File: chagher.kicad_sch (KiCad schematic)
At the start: 16 parts, among them Q2 AO3401A, U6 CN3763

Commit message: DRC check
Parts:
- L2: footprint Inductor_SMD:L_TDK_VLS6045EX_VLS6045AF -> Inductor_SMD:L_TechFuse_SL0624
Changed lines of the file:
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@@
 			)
 		)
-		(property "Footprint" "Inductor_SMD:L_TDK_VLS6045EX_VLS6045AF"
+		(property "Footprint" "Inductor_SMD:L_TechFuse_SL0624"
 			(at 178.562 69.85 0)
 			(effects

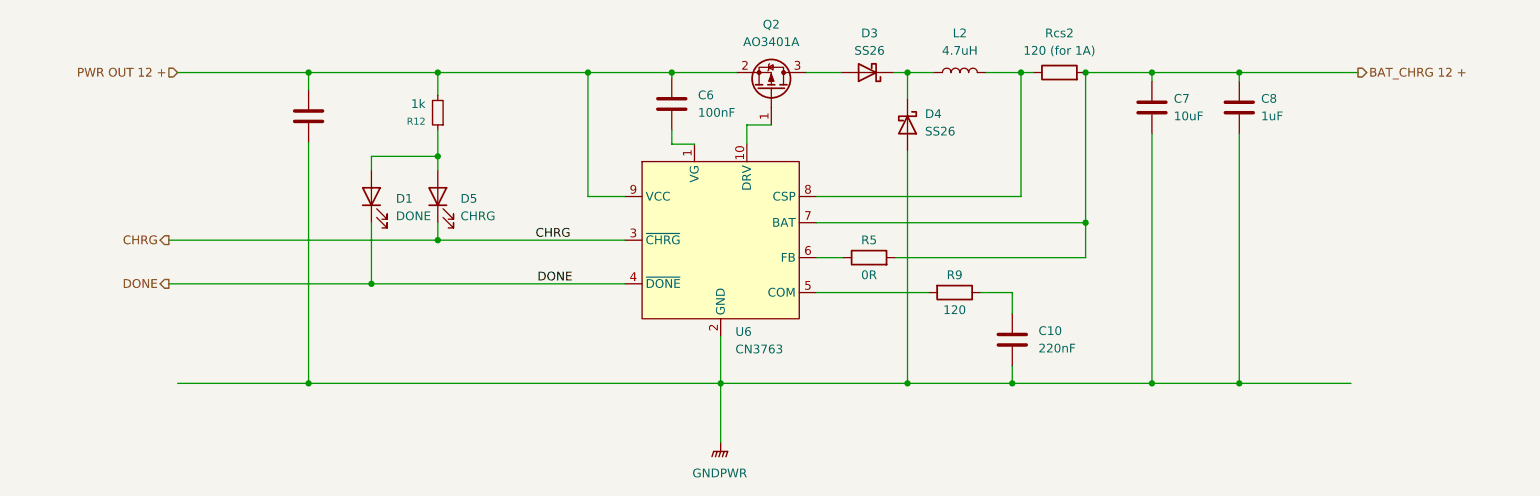
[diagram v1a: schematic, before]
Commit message: Add bat input stabilizer
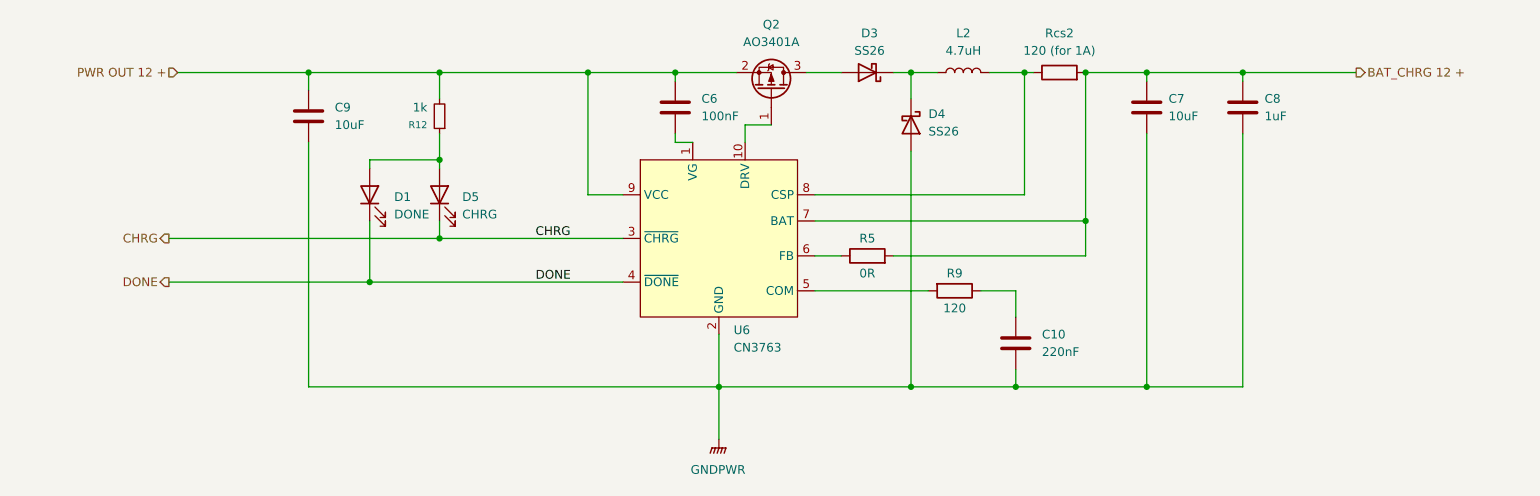
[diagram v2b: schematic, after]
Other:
- moved on the sheet: C10, C6, C7, C8, D4, L2, R12

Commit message: Add power sockwr
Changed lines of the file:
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@@
 	(wire
 		(pts
-			(xy 64.77 69.85) (xy 83.82 69.85)
+			(xy 63.5 69.85) (xy 83.82 69.85)
 		)
 		(stroke
@@
 	(hierarchical_label "PWR OUT 12 +"
 		(shape input)
-		(at 64.77 69.85 180)
+		(at 63.5 69.85 180)
 		(effects
 			(font

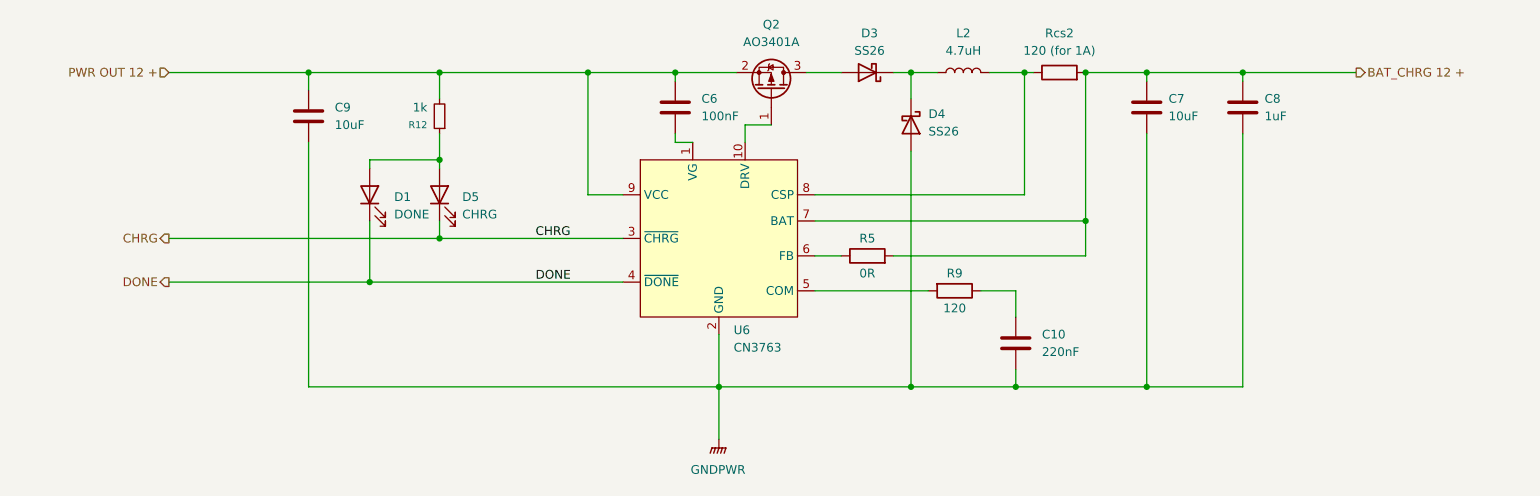
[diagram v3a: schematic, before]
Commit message: Clean space for second relay
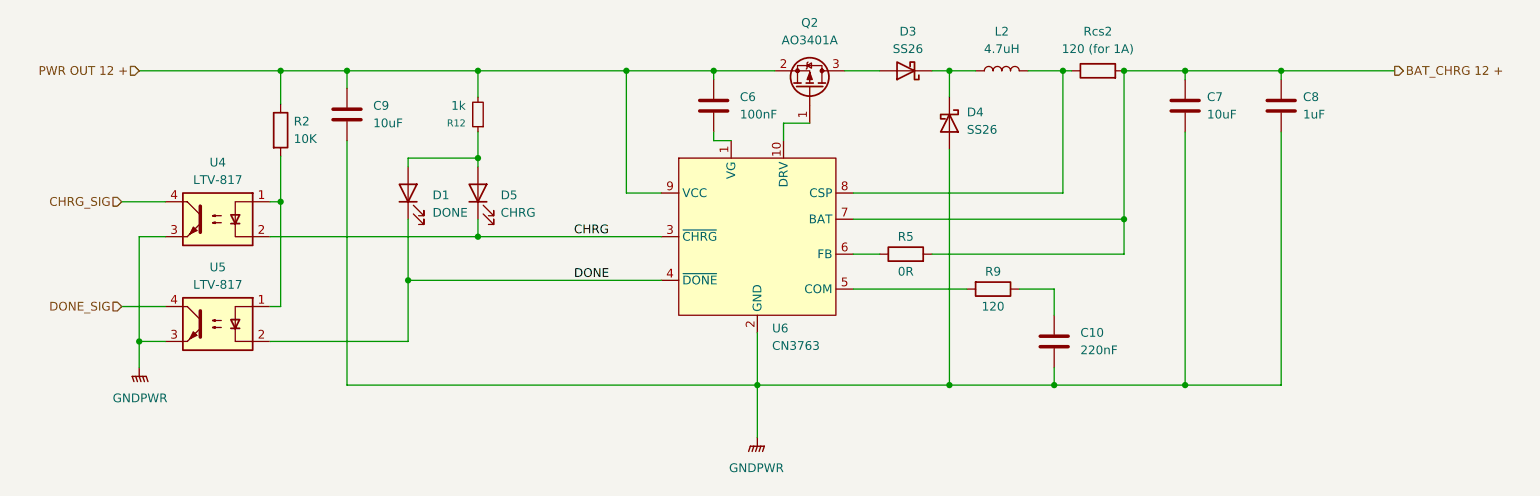
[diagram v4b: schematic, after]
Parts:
- added R2: 10K, Resistor_SMD:R_0805_2012Metric_Pad1.20x1.40mm_HandSolder, symbol Device:R
- added U4, U5: LTV-817, Package_DIP:DIP-4_W7.62mm, symbol Isolator:LTV-817
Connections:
- net CHRG: now also U4.2
- net DONE: now also U5.2
- net GNDPWR: now also U4.3, U5.3
- net PWR OUT 12 +: now also R2.1
- new net: R2.2, U4.1, U5.1
- new net CHRG_SIG: U4.4
- new net DONE_SIG: U5.4
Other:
- moved on the sheet: C10, C6, C7, C8, C9, D1, D3, D4, D5, L2, Q2, R12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
